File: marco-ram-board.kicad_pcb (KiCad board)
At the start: 4 copper layers, 160 x 100 mm, 186 parts, among them J201 PRG_USB, J202 MCU_RST, J203 MCU_BOOT0, J204 FT_TXD, J205 FT_RXD, J206 CONN_JTAG, J301 CONN_MCU_SERIAL, J302 CONN_EXT, J501 MCU_USB, J502 SD_Card, J503 CONN_DISP, J504 RJ45_Amphenol_RJMG1BD3B8K1ANR, J601 CONN_JACK_12V, J602 CONN_SCREW_12V, Q201 MMBT3906, Q601 DMP3037LSS, SW301 SW_RST, SW302 SW_BOOT0, SW501 BTN0, SW502 BTN1, SW503 BTN2, SW504 BTN3, SW601 PWR_SW, U201 FT2232HL, U301 STM32F765IITx, U401 IS42S86400D, U402 IS42S86400D, U403 IS42S86400D, U404 IS42S86400D, U405 IS42S86400D, U406 IS42S86400D, U407 IS42S86400D, U408 IS42S86400D, U501 KSZ8081RNA, U601 LM2576S-3.3, Y201 12MHz, Y301 25MHz

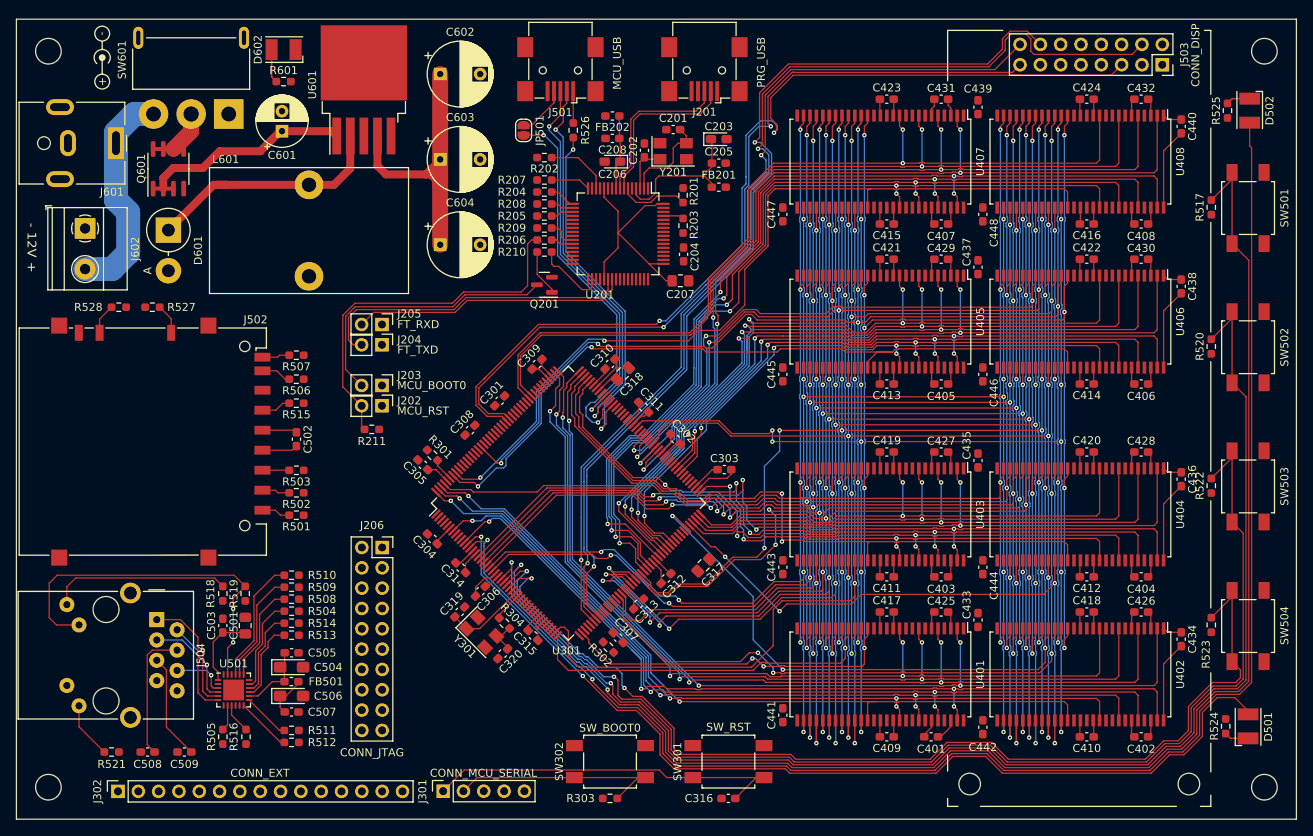
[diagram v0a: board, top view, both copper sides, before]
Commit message: Route SDMMC
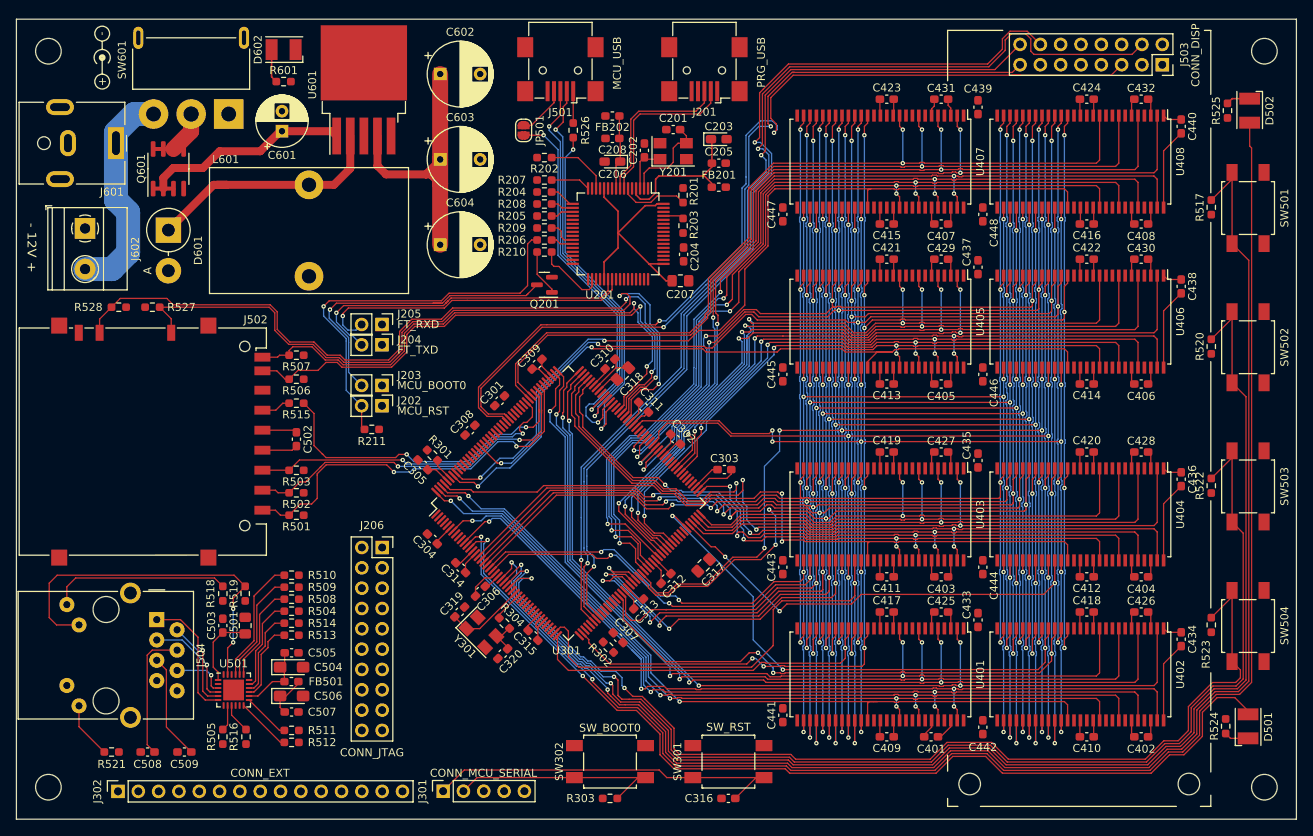
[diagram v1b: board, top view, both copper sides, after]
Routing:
- net /mcu-if/SDMMC.WP: track 3.82 -> 97.4 mm, vias 0 -> 2
- net /mcu-if/SDMMC.CD: track 3.80 -> 95.3 mm, vias 0 -> 2
- net /mcu-if/SDMMC.D1: track 3.44 -> 69.2 mm, vias 0 -> 2
- net /mcu-if/SDMMC.D0: track 3.77 -> 69.4 mm, vias 0 -> 2
- net /mcu-if/SDMMC.D2: track 3.60 -> 48.7 mm, vias 0 -> 2
- net /mcu-if/SDMMC.CK: track 0.00 -> 41.3 mm, vias 0 -> 2
- net /mcu-if/SDMMC.D3: track 3.47 -> 44.5 mm, vias 0 -> 2
- net /mcu-if/SDMMC.CMD: track 3.32 -> 40.2 mm, vias 0 -> 2
- net Net-(J205-Pad2): track 34.4 -> 40.6 mm, vias 0 -> 1
- net Net-(J203-Pad2): track 35.0 -> 39.6 mm, vias 0 -> 1
- net Net-(J202-Pad2): track 46.6 -> 50.7 mm, vias 0 -> 1
- net Net-(J204-Pad2): track 39.9 -> 42.4 mm, vias 0 -> 1
- net /mcu/SDRAM.~{BL0}: track 105.4 -> 106.4 mm
- net /mcu/SDRAM.~{CAS}: track 232.3 -> 233.0 mm
- net /mcu-if/BTN0: track 185.9 -> 186.5 mm

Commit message: Route debug JTAG and serial.
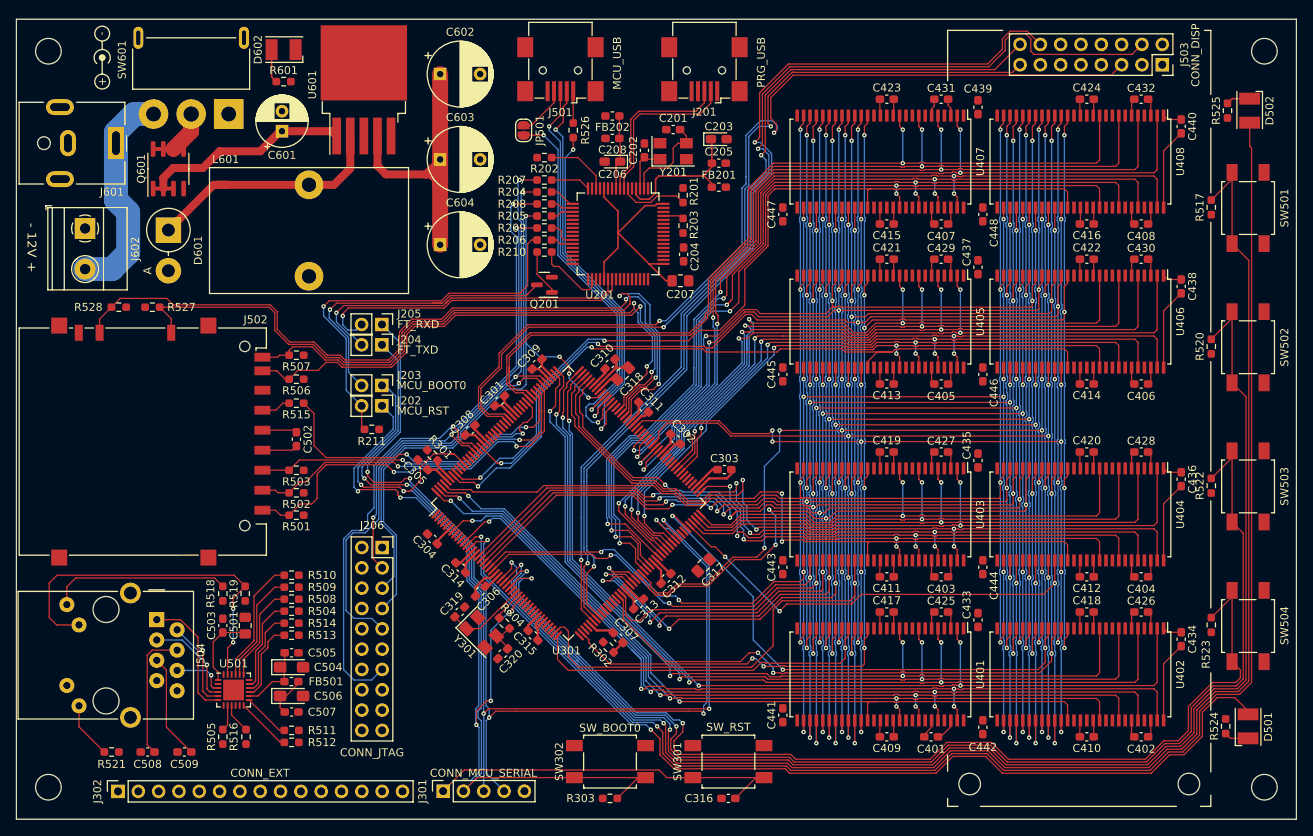
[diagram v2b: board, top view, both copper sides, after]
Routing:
- net /mcu/TXD: track 0.00 -> 129.7 mm, vias 0 -> 5
- net /mcu/RXD: track 0.00 -> 124.9 mm, vias 0 -> 5
- net /mcu/JTAG.TDO: track 0.00 -> 85.2 mm, vias 0 -> 2
- net /mcu/~{RESET}: track 46.3 -> 129.4 mm, vias 0 -> 5
- net /mcu/JTAG.TCK: track 0.00 -> 79.5 mm, vias 0 -> 2
- net /mcu/JTAG.TMS: track 0.00 -> 77.2 mm, vias 0 -> 4
- net /mcu/BOOT0: track 27.1 -> 103.0 mm, vias 0 -> 2
- net /mcu/JTAG.TDI: track 0.00 -> 68.0 mm, vias 0 -> 2
- net /mcu/JTAG.TRST: track 0.00 -> 60.5 mm, vias 0 -> 3
- net VDD: track 161.9 -> 170.7 mm
- net GND: track 147.2 -> 154.2 mm
- net /mcu/SDRAM.D2: track 109.1 -> 113.8 mm
- net /mcu/SDRAM.D3: track 106.7 -> 109.4 mm
- net /mcu-if/BTN3: track 130.2 -> 131.5 mm
- net /mcu-if/DISP.~{RST}: track 101.4 -> 102.3 mm
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
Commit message: Artwork cleanup
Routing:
- net VDD: track 170.7 -> 160.3 mm
- net GND: track 154.2 -> 147.1 mm
- net /mcu/SDRAM.D10: track 100.4 -> 98.3 mm
- net /mcu-if/DISP.MOSI: track 120.0 -> 118.4 mm
- net /mcu-if/SDMMC.D3: track 44.5 -> 43.3 mm
- net Net-(J203-Pad2): track 39.6 -> 38.3 mm
- net /mcu/SDRAM.D5: track 111.6 -> 110.8 mm
- net /mcu/SDRAM.D2: track 113.8 -> 113.0 mm
- net /mcu-if/SDMMC.D2: track 48.7 -> 48.0 mm
- net /mcu-if/SDMMC.CD: track 95.3 -> 94.7 mm
- net /mcu/BOOT0: track 103.0 -> 102.3 mm
- net /mcu-if/BTN0: track 187.2 -> 186.6 mm

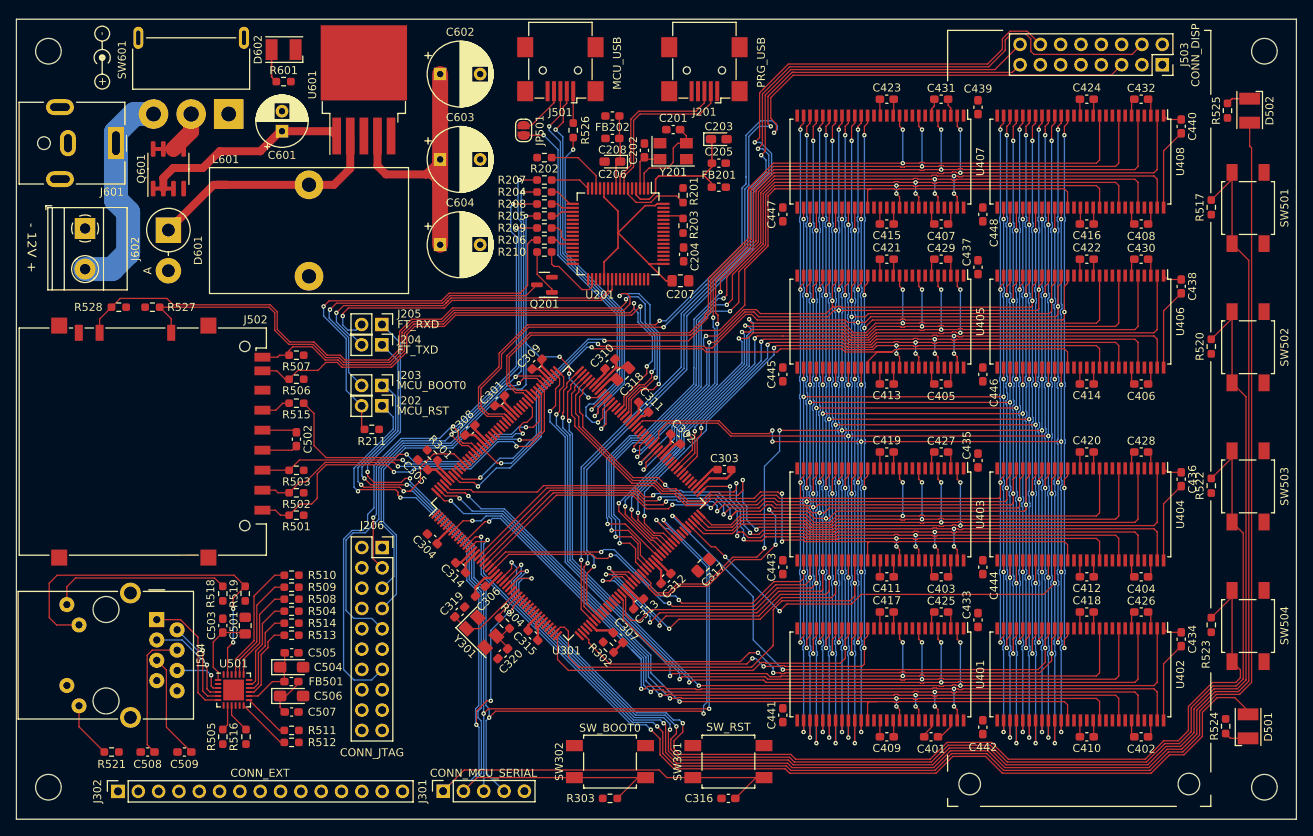
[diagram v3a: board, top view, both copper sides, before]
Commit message: Fix missing EXT9 connection, move EXT9-13 to PEx, route EXT connector.
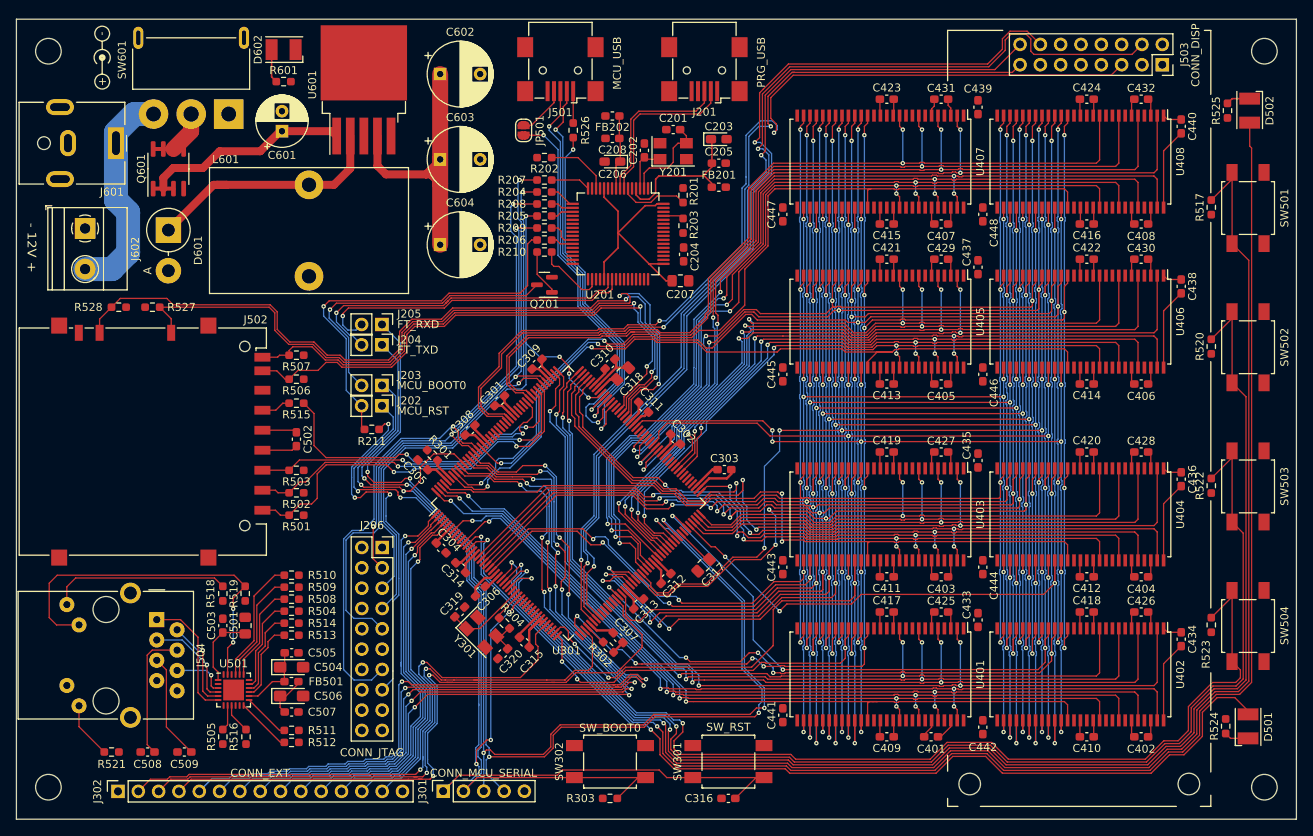
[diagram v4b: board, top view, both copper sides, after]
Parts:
- moved C304 1.57 mm to (123.1, 106.1), turned to -45 degrees
- moved C315 1.38 mm to (133.5, 117.9)
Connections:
- U301 pad 1: unconnected-(U301-Pad1) -> /mcu/EXT9
- U301 pad 2: unconnected-(U301-Pad2) -> /mcu/EXT10
- U301 pad 3: unconnected-(U301-Pad3) -> /mcu/EXT11
- U301 pad 4: unconnected-(U301-Pad4) -> /mcu/EXT12
- U301 pad 5: unconnected-(U301-Pad5) -> /mcu/EXT13
- U301 pad 92: /mcu/EXT10 -> unconnected-(U301-Pad92)
- U301 pad 93: /mcu/EXT11 -> unconnected-(U301-Pad93)
- U301 pad 94: /mcu/EXT12 -> unconnected-(U301-Pad94)
- U301 pad 95: /mcu/EXT13 -> unconnected-(U301-Pad95)
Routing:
- net /mcu/EXT4: track 0.00 -> 113.5 mm, vias 0 -> 5
- net /mcu/EXT5: track 0.00 -> 108.6 mm, vias 0 -> 5
- net /mcu/EXT6: track 0.00 -> 101.3 mm, vias 0 -> 5
- net /mcu/EXT7: track 0.00 -> 96.7 mm, vias 0 -> 5
- net /mcu/EXT8: track 0.00 -> 93.6 mm, vias 0 -> 5
- net /mcu/EXT3: track 0.00 -> 84.1 mm, vias 0 -> 2
- net /mcu/EXT2: track 0.00 -> 76.5 mm, vias 0 -> 2
- net /mcu/EXT1: track 0.00 -> 73.3 mm, vias 0 -> 2
- net /mcu/EXT9: track 0.00 -> 50.4 mm, vias 0 -> 1
- net /mcu/EXT10: track 0.00 -> 47.0 mm, vias 0 -> 1
- net /mcu/EXT11: track 0.00 -> 44.1 mm, vias 0 -> 1
- net Net-(J206-Pad15): track 0.00 -> 43.7 mm, vias 0 -> 3
- net /mcu/EXT12: track 0.00 -> 41.7 mm, vias 0 -> 1
- net /mcu/EXT13: track 0.00 -> 39.4 mm, vias 0 -> 1
- net /mcu/RXD: track 124.9 -> 138.0 mm
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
